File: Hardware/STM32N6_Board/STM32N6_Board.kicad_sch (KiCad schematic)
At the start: 0 parts

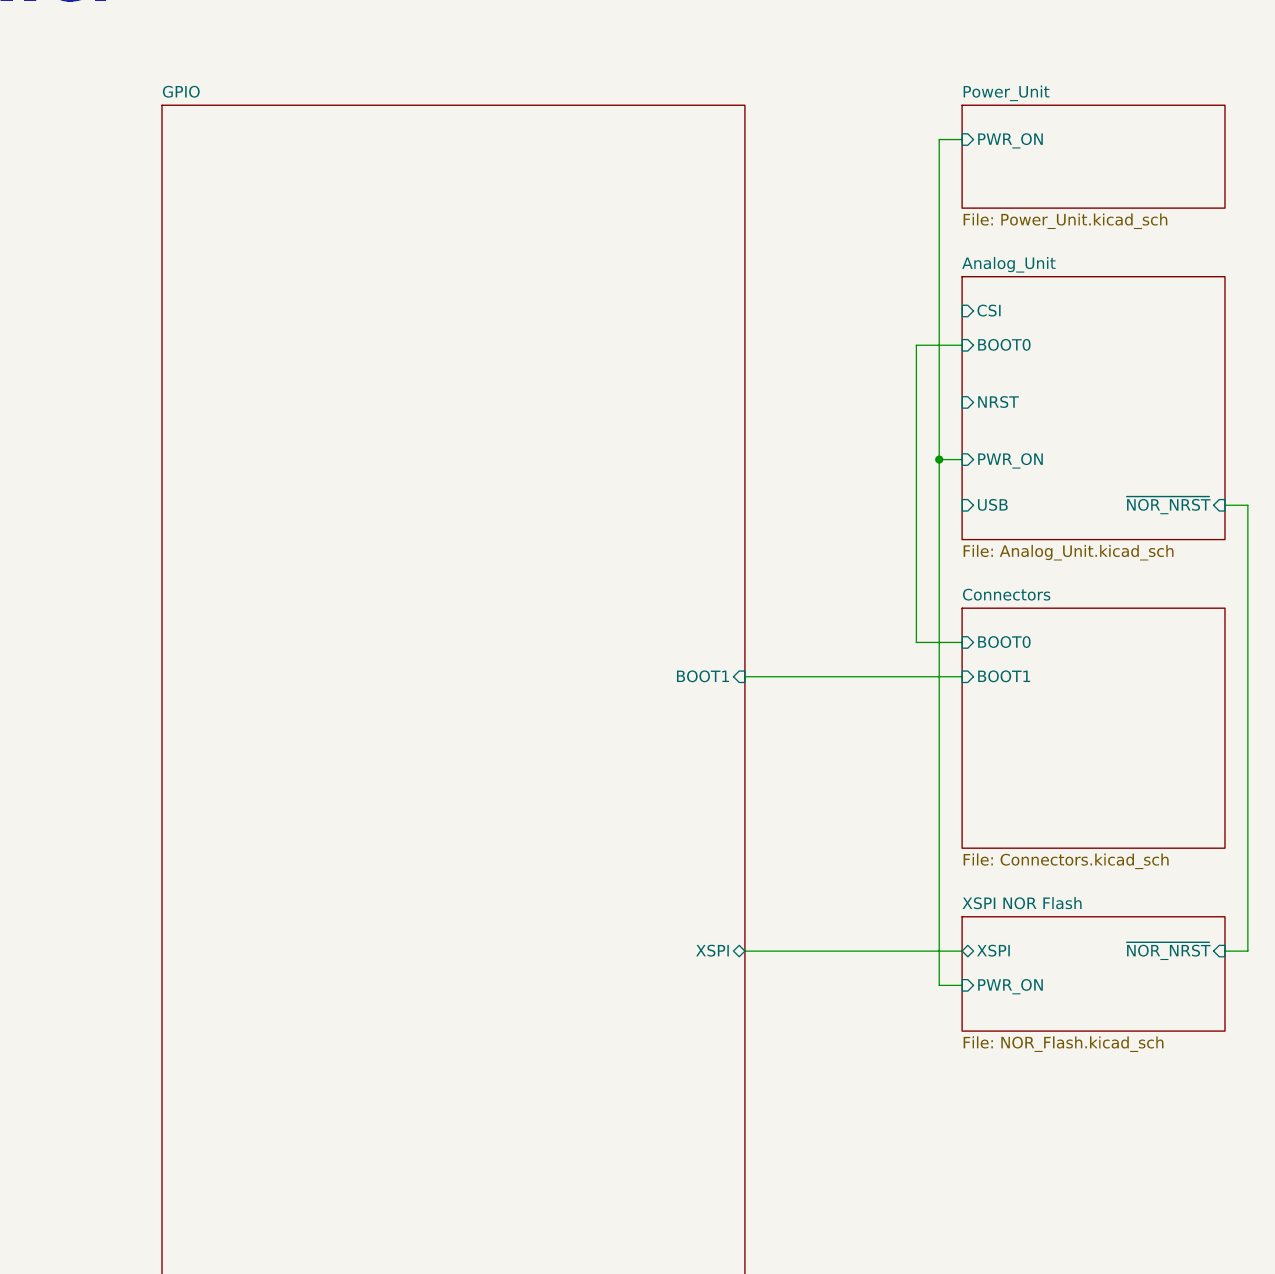
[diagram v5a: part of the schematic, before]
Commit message: Added pinout to GPIO
- Had to rearrange the pinout a little, due to SPI NSS issue
- New pinout updated in google spreadsheet and image in docs
- Added buses in GPIO sheet, as well as all necessary labels
- Next is wiring in FMC SDRAM, and connectors.
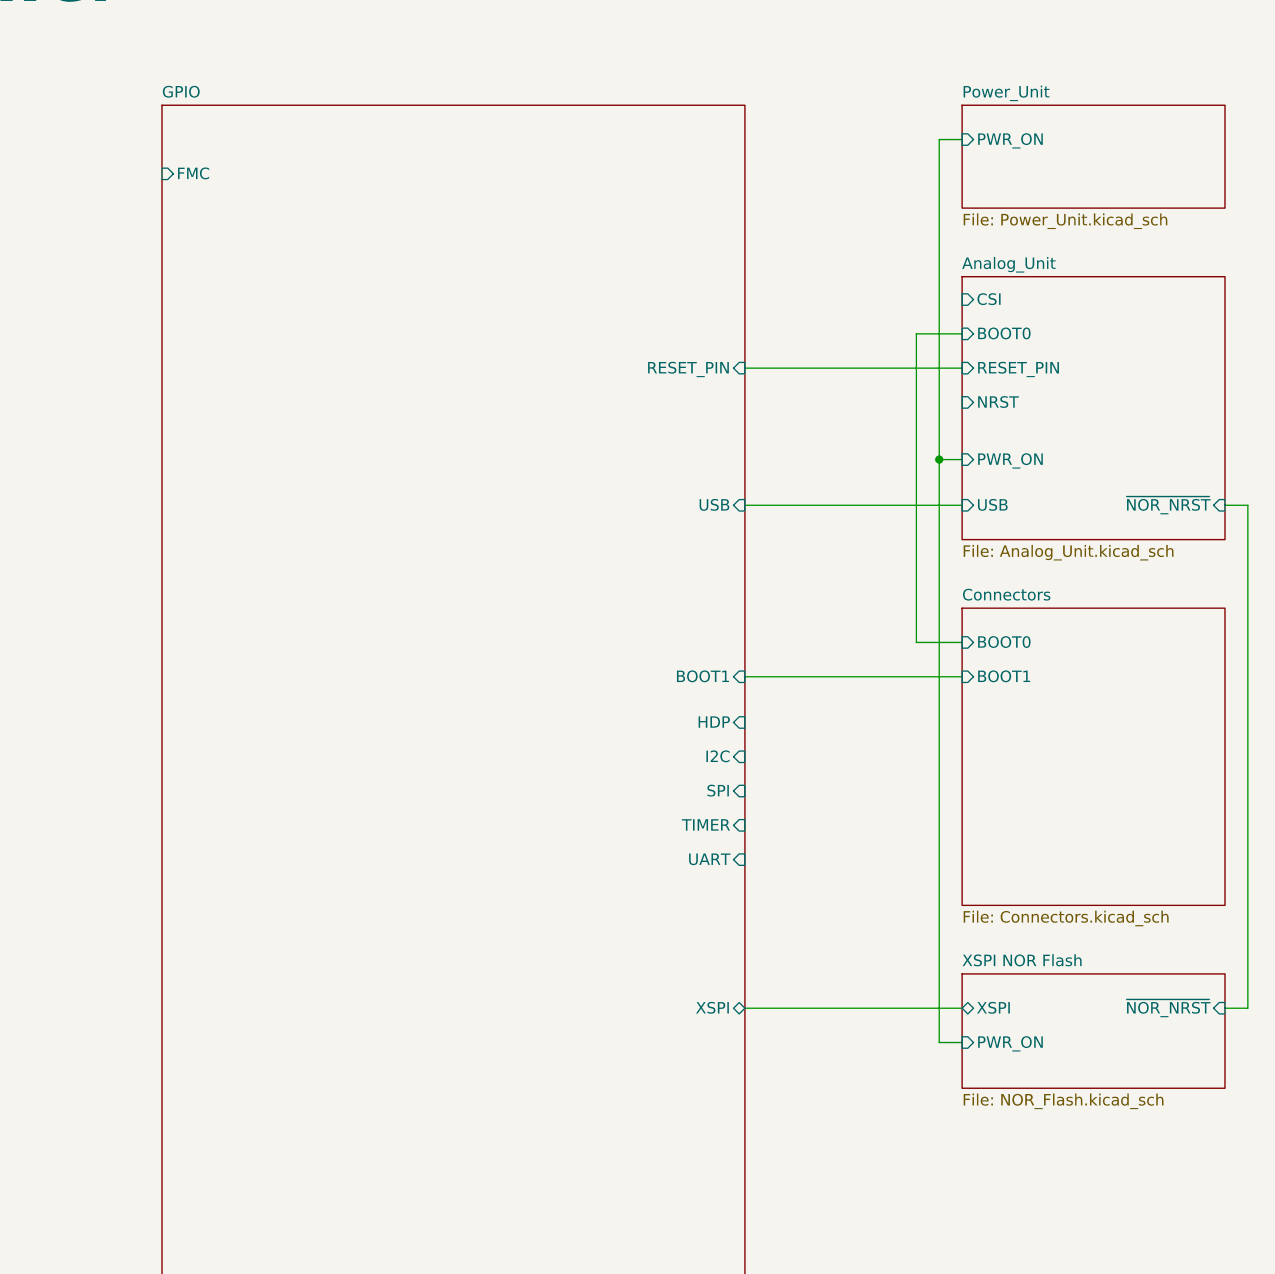
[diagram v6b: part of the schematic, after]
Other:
- sheet Analog_Unit ports: added RESET_PIN; removed none
- sheet GPIO ports: added FMC, HDP, I2C, RESET_PIN, SPI, TIMER, UART, USB; removed none
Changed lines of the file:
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@@
 	(wire
 		(pts
-			(xy 217.17 146.05) (xy 214.63 146.05)
+			(xy 217.17 152.4) (xy 214.63 152.4)
+		)
+		(stroke
+			(width 0)
+			(type default)
+		)
+	)
+	(wire
+		(pts
+			(xy 161.29 81.28) (xy 185.42 81.28)
 		)
 		(stroke
@@
 	(wire
 		(pts
-			(xy 182.88 149.86) (xy 182.88 91.44)
-		)
-		(stroke
-			(width 0)
-			(type default)
-		)
-	)
-	(wire
-		(pts
-			(xy 180.34 78.74) (xy 180.34 111.76)
-		)
-		(stroke
-			(width 0)
-			(type default)
-		)
-	)
-	(wire
-		(pts
-			(xy 161.29 146.05) (xy 185.42 146.05)
-		)
-		(stroke
-			(width 0)
-			(type default)
-		)
-	)
-	(wire
-		(pts
-			(xy 185.42 149.86) (xy 182.88 149.86)
+			(xy 182.88 156.21) (xy 182.88 91.44)
+		)
+		(stroke
+			(width 0)
+			(type default)
+		)
+	)
+	(wire
+		(pts
+			(xy 180.34 77.47) (xy 180.34 111.76)
+		)
+		(stroke
+			(width 0)
+			(type default)
+		)
+	)
+	(wire
+		(pts
+			(xy 161.29 96.52) (xy 185.42 96.52)
+		)
+		(stroke
+			(width 0)
+			(type default)
+		)
+	)
+	(wire
+		(pts
+			(xy 161.29 152.4) (xy 185.42 152.4)
+		)
+		(stroke
+			(width 0)
+			(type default)
+		)
+	)
+	(wire
+		(pts
+			(xy 185.42 156.21) (xy 182.88 156.21)
 		)
 		(stroke
@@
 	(wire
 		(pts
-			(xy 185.42 78.74) (xy 180.34 78.74)
+			(xy 185.42 77.47) (xy 180.34 77.47)
 		)
 		(stroke
@@
 	(wire
 		(pts
-			(xy 217.17 96.52) (xy 217.17 146.05)
+			(xy 217.17 96.52) (xy 217.17 152.4)
 		)
 		(stroke
@@
 		)
 		(pin "XSPI" bidirectional
-			(at 161.29 146.05 0)
+			(at 161.29 152.4 0)
 			(effects
 				(font
@@
 		(pin "BOOT1" input
 			(at 161.29 115.57 0)
+			(effects
+				(font
+					(size 1.27 1.27)
+				)
+				(justify right)
+			)
+		)
+		(pin "USB" input
+			(at 161.29 96.52 0)
+			(effects
+				(font
+					(size 1.27 1.27)
+				)
+				(justify right)
+			)
+		)
+		(pin "RESET_PIN" input
+			(at 161.29 81.28 0)
+			(effects
+				(font
+					(size 1.27 1.27)
+				)
+				(justify right)
+			)
+		)
+		(pin "FMC" input
+			(at 96.52 59.69 180)
+			(effects
+				(font
+					(size 1.27 1.27)
+				)
+				(justify left)
+			)
+		)
+		(pin "HDP" input
+			(at 161.29 120.65 0)
+			(effects
+				(font
+					(size 1.27 1.27)
+				)
+				(justify right)
+			)
+		)
+		(pin "I2C" input
+			(at 161.29 124.46 0)
+			(effects
+				(font
+					(size 1.27 1.27)
+				)
+				(justify right)
+			)
+		)
+		(pin "SPI" input
+			(at 161.29 128.27 0)
+			(effects
+				(font
+					(size 1.27 1.27)
+				)
+				(justify right)
+			)
+		)
+		(pin "TIMER" input
+			(at 161.29 132.08 0)
+			(effects
+				(font
+					(size 1.27 1.27)
+				)
+				(justify right)
+			)
+		)
+		(pin "UART" input
+			(at 161.29 135.89 0)
 			(effects
 				(font
@@
 	)
 	(sheet
-		(at 185.42 142.24)
+		(at 185.42 148.59)
 		(size 29.21 12.7)
 		(exclude_from_sim no)
@@
 		)
 		(property "Sheetname" "XSPI NOR Flash"
-			(at 185.42 141.5284 0)
+			(at 185.42 147.8784 0)
 			(effects
 				(font
@@
 		)
 		(property "Sheetfile" "NOR_Flash.kicad_sch"
-			(at 185.42 155.5246 0)
+			(at 185.42 161.8746 0)
 			(effects
 				(font
@@
 		)
 		(pin "XSPI" bidirectional
-			(at 185.42 146.05 180)
+			(at 185.42 152.4 180)
 			(effects
 				(font
@@
 		)
 		(pin "PWR_ON" input
-			(at 185.42 149.86 180)
+			(at 185.42 156.21 180)
 			(effects
 				(font
@@
 		)
 		(pin "~{NOR_NRST}" input
-			(at 214.63 146.05 0)
+			(at 214.63 152.4 0)
 			(effects
 				(font
@@
 		)
 		(pin "BOOT0" input
-			(at 185.42 78.74 180)
+			(at 185.42 77.47 180)
 			(effects
 				(font
@@
 		)
 		(pin "CSI" input
-			(at 185.42 74.93 180)
+			(at 185.42 73.66 180)
 			(effects
 				(font
@@
 				)
 				(justify right)
+			)
+		)
+		(pin "RESET_PIN" input
+			(at 185.42 81.28 180)
+			(effects
+				(font
+					(size 1.27 1.27)
+				)
+				(justify left)
 			)
 		)
@@
 	(sheet
 		(at 185.42 107.95)
-		(size 29.21 26.67)
+		(size 29.21 33.02)
 		(exclude_from_sim no)
 		(in_bom yes)
@@
 		)
 		(property "Sheetfile" "Connectors.kicad_sch"
-			(at 185.42 135.2046 0)
-			(effects
-				(font
+			(at 185.42 141.5546 0)
+			(effects
+				(font

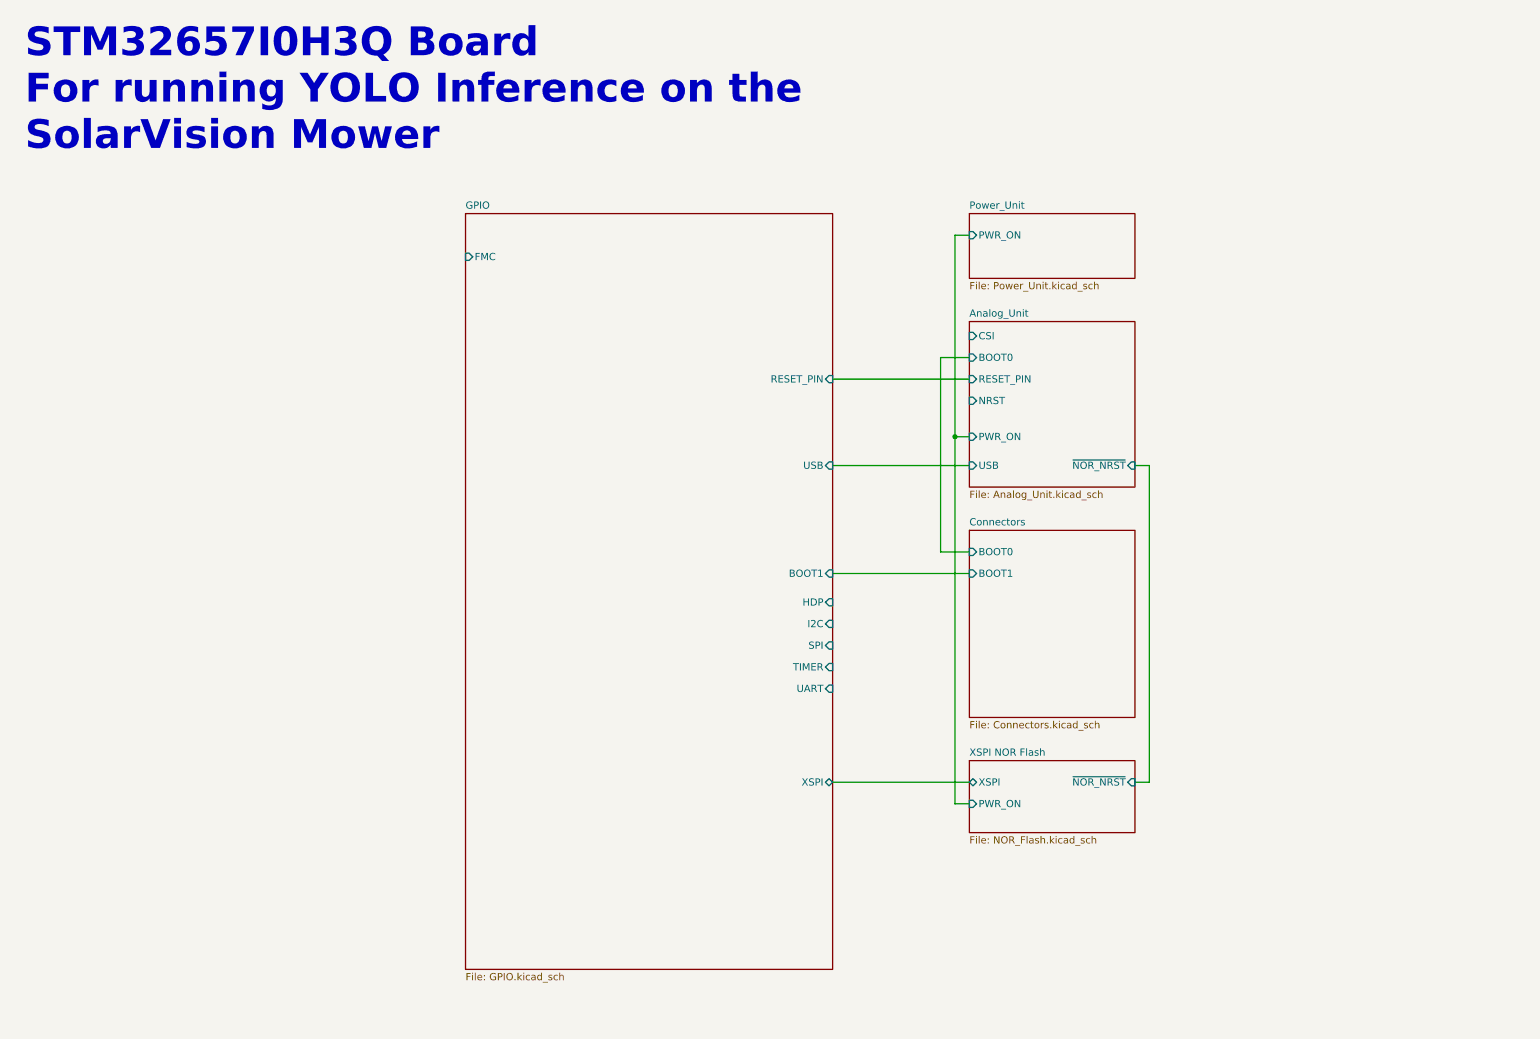
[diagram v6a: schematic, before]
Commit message: Completed the schematic.
- The schematic is complete.
- ERC checker, footprint assignment, and PCB board design left
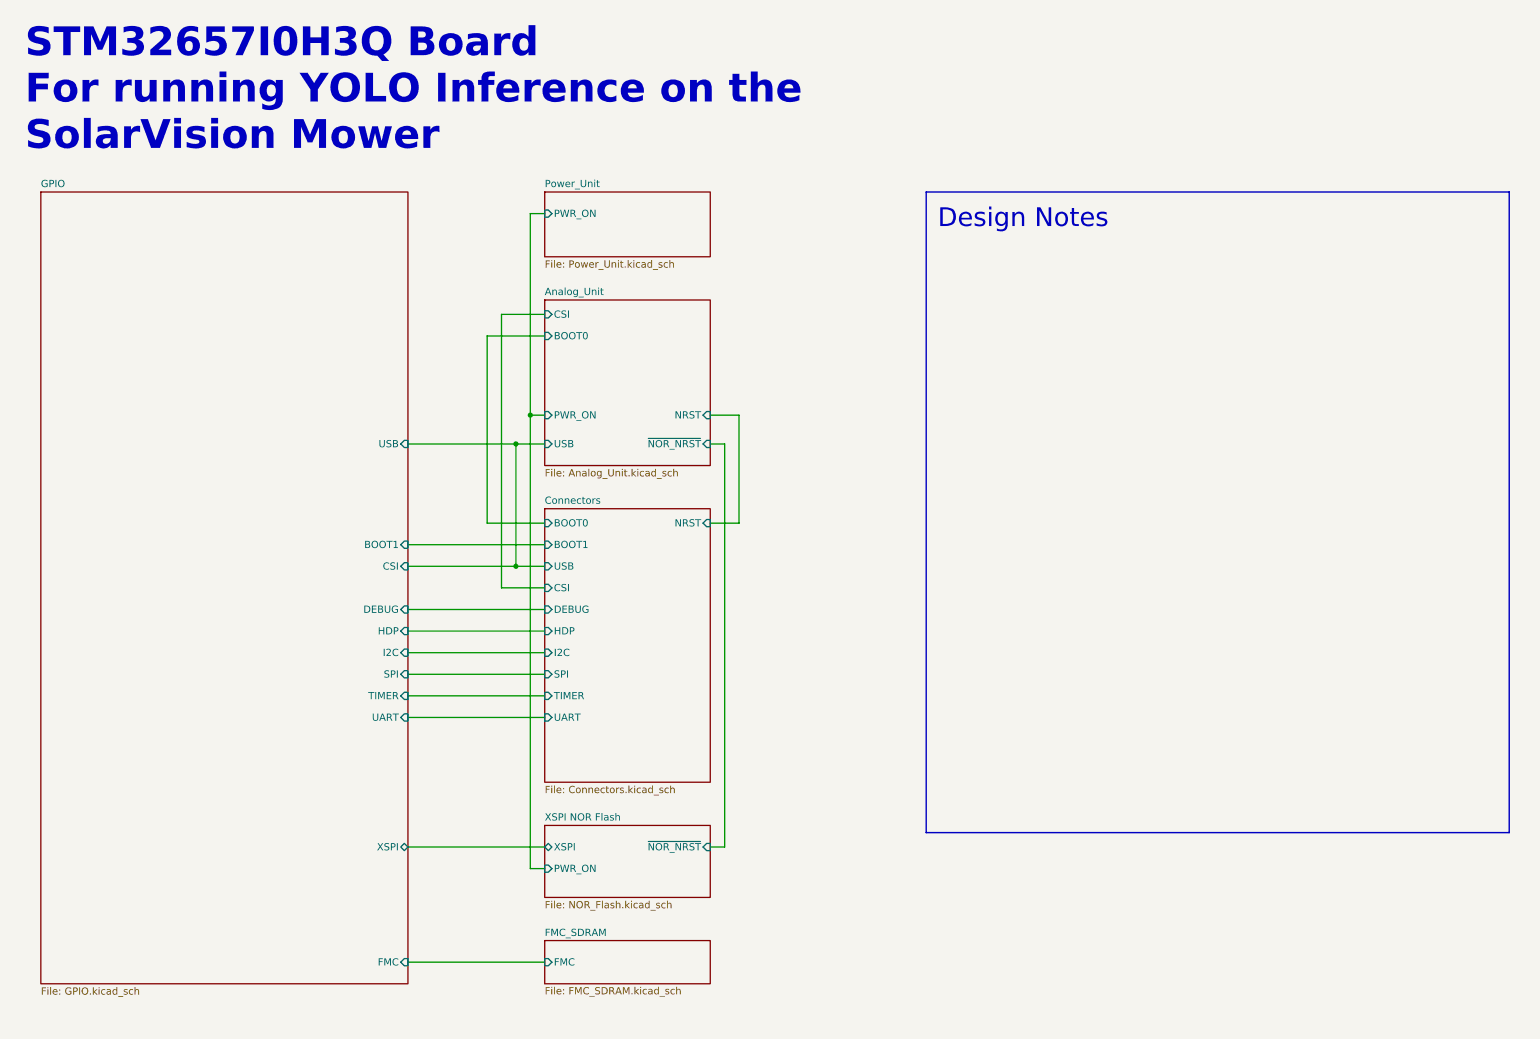
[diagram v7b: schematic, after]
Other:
- added sheet FMC_SDRAM (FMC_SDRAM.kicad_sch)
- sheet Analog_Unit ports: added none; removed RESET_PIN
- sheet Connectors ports: added CSI, DEBUG, HDP, I2C, NRST, SPI, TIMER, UART, USB; removed none
- sheet GPIO ports: added CSI, DEBUG; removed RESET_PIN
- note added: "Design Notes"

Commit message: Fixed a tiny issue
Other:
- note removed: "Design Notes"
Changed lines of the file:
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@@
 		(comment 1 "https://github.com/SolarVisionMower/SolarVision")
-	)
-	(rectangle
-		(start 177.8 48.26)
-		(end 280.67 161.29)
-		(stroke
-			(width 0.254)
-			(type solid)
-		)
-		(fill
-			(type none)
-		)
-	)
-	(text "Design Notes"
-		(exclude_from_sim no)
-		(at 179.832 51.054 0)
-		(effects
-			(font
-				(size 3.302 3.302)
-				(thickness 0.4128)
-			)
-			(justify left top)
-		)
 	)
 	(text "STM32657I0H3Q Board\nFor running YOLO Inference on the\nSolarVision Mower"
